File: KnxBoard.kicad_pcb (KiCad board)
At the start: 4 copper layers, 35.8 x 33.8 mm, 44 parts, among them IC1 STM32G491KEU6, IC2 NCN5130MNTWG, J1 Conn_01x02, J2 Conn_02x03_Counter_Clockwise, J3 Conn_01x10, J4 Conn_01x10, SW1 SW_Push, Y1 16MHz

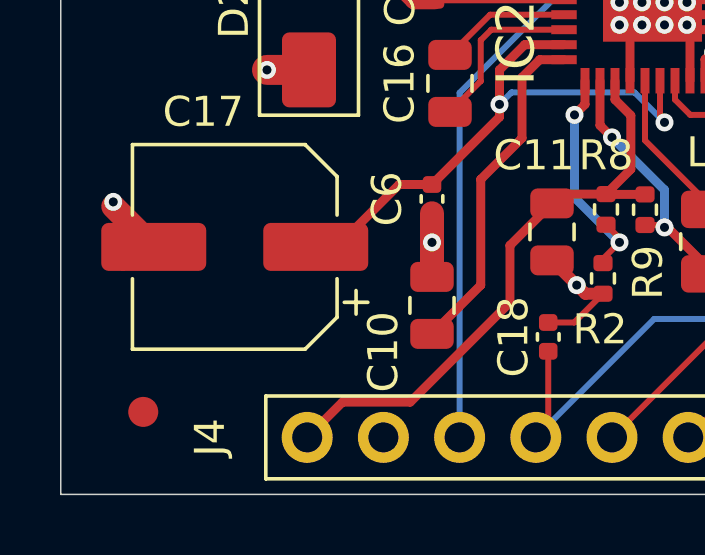
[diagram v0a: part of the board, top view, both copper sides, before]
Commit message: Add new capa footprint on the other side
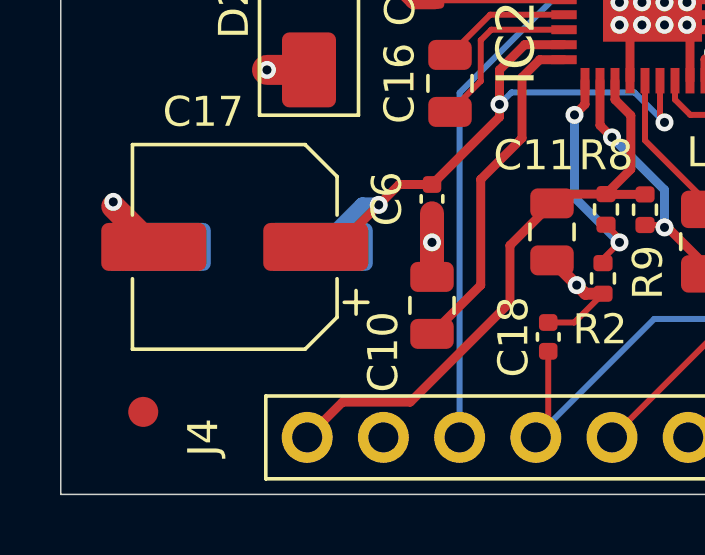
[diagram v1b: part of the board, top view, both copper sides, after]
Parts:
- added C19: 100uF 35 Volt, Capacitor_SMD:CP_Elec_6.3x7.7, B.Cu at (127.1, 151.4)
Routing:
- net Net-(IC2-VFILT): track 19.5 -> 22.1 mm, vias 2 -> 3
- net GND: track 67.5 -> 69.6 mm
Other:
- board text removed: "Fabien"
- board text removed: "Proriol"
